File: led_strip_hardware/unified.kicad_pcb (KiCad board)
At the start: 4 copper layers, 48.3 x 20.3 mm, 39 parts, among them P1 mod_jack_in, P2 PWR_TST, P3 LED_STRIP, P4 ICSP, Q1 FDN5618P, SW1 USR_SW, U1 ISL83485IBZ, U2 TPS54560, U3 STM32F030-32, U4 NCP1117ST33T3G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

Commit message: LED strip hardware rev 7; ready for prod?
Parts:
- C1, C10: footprint SM1210 -> Capacitors_SMD:C_1210
- C11, C9: footprint SA0805 -> Capacitors_SMD:C_0805
- C12, C2, C3, C4, C5, C8, R10, R2, R3, R4, R5, R6, R7, R8, R9: footprint SA0402 -> Resistors_SMD:R_0402
- R1, R11, R12: footprint SA0603 -> Resistors_SMD:R_0603
- U4: value NCP1117ST33T3G -> 1117
- moved Q1 0.80 mm to (121.4, 121.4)
- moved C6 0.76 mm to (152.4, 119.9)
- moved D2 0.51 mm to (132.6, 112.8)
- moved R9 0.38 mm to (118.5, 122.2)
- moved R10 0.25 mm to (117.1, 122.2)
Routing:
- net GND: track 115.0 -> 103.8 mm, vias 50 -> 40
- net VPP: track 47.5 -> 37.3 mm, vias 3 -> 4
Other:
- board size 48.3 x 20.3 mm -> 48.3 x 26.9 mm
- board text added: "LUX"

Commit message: More 'final' touches
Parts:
- D1: footprint SA0603_LED -> LEDs:LED_0603
- moved R7 2.54 mm to (154.9, 115.6), turned to 270 degrees
- moved R8 2.54 mm to (154.9, 118.1), turned to 90 degrees
- moved R5 1.40 mm to (128.4, 125.0), turned to 90 degrees
- moved R6 1.14 mm to (127.1, 125.0)
- moved C4 0.13 mm to (130.9, 125.0), turned to 90 degrees
- moved R3 0.13 mm to (129.7, 125.0)
- moved R2 0.13 mm to (125.9, 125.0)
- moved C5 0.13 mm to (132.2, 125.0)
- turned P3 to 90 degrees
- turned R10 to 90 degrees
- turned SW1 to 180 degrees
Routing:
- net VPP: track 37.3 -> 21.9 mm, vias 4 -> 3
- net GND: track 103.8 -> 111.0 mm, vias 40 -> 38
- net Net-(SW1-Pad3): track 4.53 -> 11.3 mm
- net /DAT: track 16.2 -> 15.3 mm
- net /CLK: track 13.2 -> 13.8 mm
- net Net-(R5-Pad2): track 7.17 -> 7.82 mm
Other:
- board size 48.3 x 26.9 mm -> 48.3 x 20.3 mm

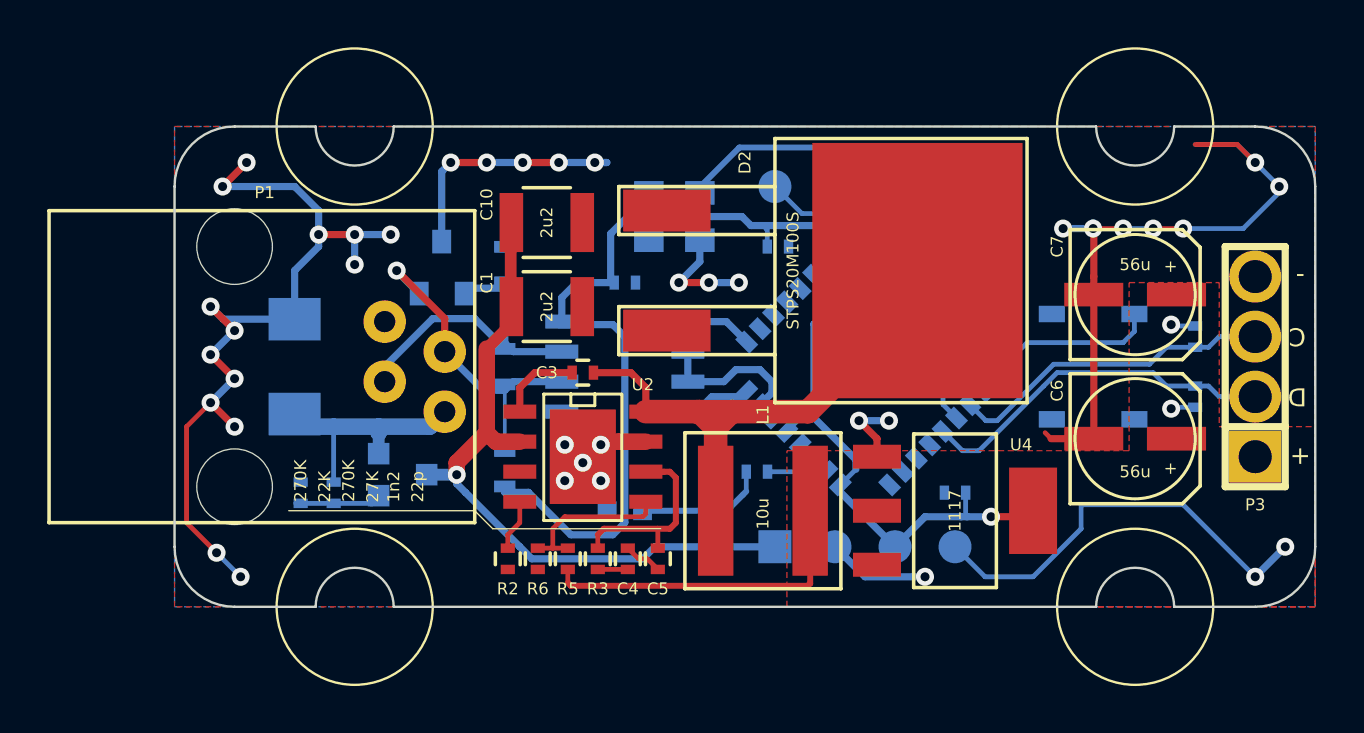
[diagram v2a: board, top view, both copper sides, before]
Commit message: Flipped D2; still need to fix silk bottom
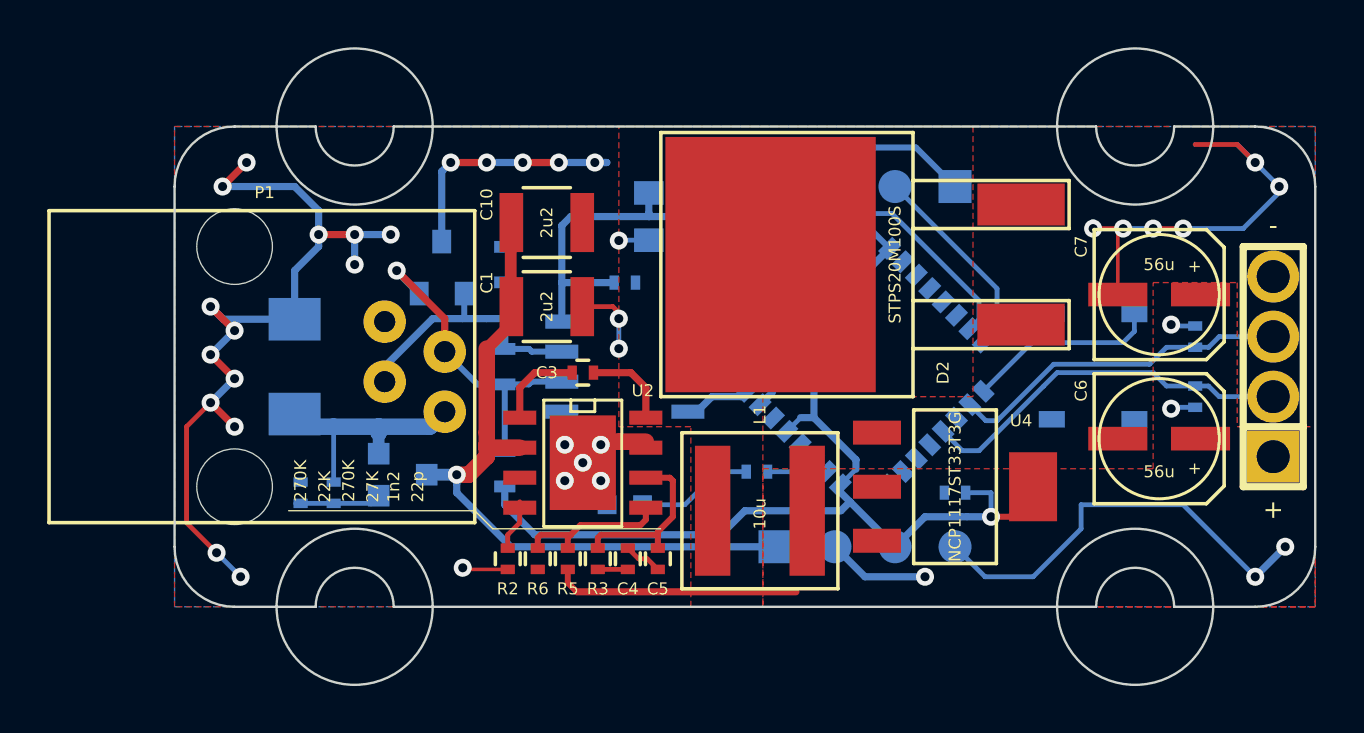
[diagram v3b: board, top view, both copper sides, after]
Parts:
- SW1: value USR_SW -> TL3315NF160Q
- U4: value 1117 -> NCP1117ST33T3G
- moved D2 15.0 mm to (147.6, 112.5), turned to 90 degrees
- moved U4 1.02 mm to (144.8, 121.9)
- moved C6 1.02 mm to (153.4, 119.9)
- moved C7 1.02 mm to (153.4, 113.8)
- moved P3 0.76 mm to (158.2, 116.8)
- moved D1 0.25 mm to (130.8, 122.7)
- moved U2 0.25 mm to (129.0, 120.9)
- moved L1 0.13 mm to (136.5, 122.9)
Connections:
- U3 pad 25: Net-(U3-Pad25) -> Net-(SW1-Pad3)
- U3 pad 27: Net-(SW1-Pad3) -> Net-(U3-Pad27)
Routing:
- net Net-(C3-Pad2): track 24.3 -> 4.40 mm
- net GND: track 111.0 -> 100.3 mm, vias 38 -> 36
- net 3V3: track 78.2 -> 83.8 mm
- net VPP: track 21.9 -> 18.3 mm
- net Net-(SW1-Pad3): track 11.3 -> 8.11 mm
- net Net-(R5-Pad2): track 7.82 -> 6.45 mm
- net Net-(C5-Pad1): track 8.69 -> 7.34 mm
- net /DAT: track 15.3 -> 16.1 mm
- net /CLK: track 13.8 -> 14.6 mm
- net Net-(P1-Pad3): track 13.7 -> 13.0 mm
- net Net-(D1-Pad1): track 5.31 -> 4.71 mm
- added copper zone on F.Cu, net Net-(C3-Pad2)
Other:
- board size 48.3 x 20.3 mm -> 48.3 x 26.9 mm

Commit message: lgtm
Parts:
- U5: value 2CH-TVS -> TVS
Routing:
- net GND: track 100.3 -> 101.8 mm, vias 36 -> 34

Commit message: ship it
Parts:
- U1: value ISL83485IBZ -> ISL83485
- U4: value NCP1117ST33T3G -> NCP1117
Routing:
- net VPP: track 18.3 -> 23.1 mm
- net GND: track 101.8 -> 104.5 mm, vias 34 -> 35
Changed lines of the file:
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@@
     (links 115)
     (no_connects 0)
-    (area 111.709999 103.327999 160.070001 130.352001)
+    (area 97.977143 98.75 160.070001 130.352001)
     (thickness 1.6)
     (drawings 48)
-    (tracks 315)
+    (tracks 323)
     (zones 0)
     (modules 39)
@@
   )
   (setup
-    (last_trace_width 0.1524)
+    (last_trace_width 0.5)
     (user_trace_width 0.2032)
     (user_trace_width 0.254)
@@
     (mod_text_size 0.508 0.508)
     (mod_text_width 0.0762)
-    (pad_size 1.016 2.032)
-    (pad_drill 0)
+    (pad_size 2.2 2.2)
+    (pad_drill 1.4)
     (pad_to_mask_clearance 0)
     (aux_axis_origin 150.622 110.998)
@@
     (fp_circle (center 0 0) (end 0.127 -2.54) (layer F.SilkS) (width 0.127))
     (pad 1 smd rect (at -1.75 0 180) (size 2.5 1) (layers F.Cu F.Paste F.Mask)
-      (net 8 VPP))
+      (net 8 VPP) (thermal_width 0.508))
     (pad 2 smd rect (at 1.75 0 180) (size 2.5 1) (layers F.Cu F.Paste F.Mask)
-      (net 7 GND))
+      (net 7 GND) (thermal_width 0.381))
     (model discret/c_vert_c1v5.wrl
       (at (xyz 0 0 0))
@@
       (effects (font (size 0.508 0.508) (thickness 0.0762)))
     )
-    (fp_text value NCP1117ST33T3G (at 0 0 270) (layer F.SilkS)
+    (fp_text value NCP1117 (at 0 0 270) (layer F.SilkS)
       (effects (font (size 0.508 0.508) (thickness 0.0762)))
     )
@@
     (fp_circle (center 0 0) (end 0.127 -2.54) (layer F.SilkS) (width 0.127))
     (pad 1 smd rect (at -1.75 0 180) (size 2.5 1) (layers F.Cu F.Paste F.Mask)
-      (net 8 VPP))
+      (net 8 VPP) (thermal_width 0.381))
     (pad 2 smd rect (at 1.75 0 180) (size 2.5 1) (layers F.Cu F.Paste F.Mask)
-      (net 7 GND))
+      (net 7 GND) (thermal_width 0.381))
     (model discret/c_vert_c1v5.wrl
       (at (xyz 0 0 0))
@@
     (fp_line (start -2.54 1.27) (end -2.54 -1.27) (layer F.SilkS) (width 0.3048))
     (pad 1 thru_hole rect (at -3.81 0 90) (size 2.2 2.2) (drill 1.4) (layers *.Cu *.Mask F.SilkS)
-      (net 8 VPP) (thermal_width 1.27))
+      (net 8 VPP) (zone_connect 1) (thermal_width 1.27))
     (pad 2 thru_hole circle (at -1.27 0 90) (size 2.2 2.2) (drill 1.4) (layers *.Cu *.Mask F.SilkS)
       (net 3 /DAT))
@@
       (effects (font (size 0.508 0.508) (thickness 0.0762)) (justify mirror))
     )
-    (fp_text value ISL83485IBZ (at 0 -1.016 270) (layer B.SilkS)
+    (fp_text value ISL83485 (at 0 -1.016 270) (layer B.SilkS)
       (effects (font (size 0.508 0.508) (thickness 0.0762)) (justify mirror))
     )
@@
   (segment (start 140.589 120.777) (end 140.589 121.180797) (width 0.3048) (layer B.Cu) (net 6))
   (segment (start 138.811 118.999) (end 140.589 120.777) (width 0.3048) (layer B.Cu) (net 6))
+  (segment (start 131.699 120.269) (end 129.667 120.269) (width 0.5) (layer F.Cu) (net 7) (status C00000))
+  (segment (start 129.667 120.269) (end 129.032 120.904) (width 0.5) (layer F.Cu) (net 7) (status C00000))
+  (segment (start 151.666 119.888) (end 151.666 118.519) (width 0.1524) (layer F.Cu) (net 7))
+  (via (at 151.003 118.237) (size 0.762) (drill 0.381) (layers F.Cu B.Cu) (net 7))
+  (segment (start 151.384 118.237) (end 151.003 118.237) (width 0.1524) (layer F.Cu) (net 7))
+  (segment (start 151.666 118.519) (end 151.384 118.237) (width 0.1524) (layer F.Cu) (net 7))
   (segment (start 128.143 118.745) (end 129.921 118.745) (width 0.2032) (layer B.Cu) (net 7))
   (via (at 130.429 116.078) (size 0.762) (drill 0.381) (layers F.Cu B.Cu) (net 7))
@@
   (via (at 123.952 125.349) (size 0.762) (drill 0.381) (layers F.Cu B.Cu) (net 7))
   (segment (start 125.857 125.418) (end 124.021 125.418) (width 0.1524) (layer F.Cu) (net 7))
-  (segment (start 151.666 113.792) (end 151.666 111.224) (width 0.1524) (layer F.Cu) (net 7))
+  (segment (start 151.666 113.792) (end 151.666 111.224) (width 0.1524) (layer F.Cu) (net 7) (status 10))
   (segment (start 151.666 111.224) (end 151.892 110.998) (width 0.1524) (layer F.Cu) (net 7))
   (segment (start 157.48 108.204) (end 156.718 107.442) (width 0.2032) (layer B.Cu) (net 7))
@@
   (segment (start 119.38 111.252) (end 119.38 112.522) (width 0.3048) (layer B.Cu) (net 7))
   (via (at 119.38 112.522) (size 0.762) (drill 0.381) (layers F.Cu B.Cu) (net 7))
-  (segment (start 116.84 109.22) (end 113.792 109.22) (width 0.3048) (layer B.Cu) (net 7))
+  (segment (start 116.205 109.22) (end 113.792 109.22) (width 0.3048) (layer B.Cu) (net 7))
   (via (at 113.792 109.22) (size 0.762) (drill 0.381) (layers F.Cu B.Cu) (net 7))
   (segment (start 113.792 109.22) (end 114.808 108.204) (width 0.3048) (layer F.Cu) (net 7))
   (via (at 114.808 108.204) (size 0.762) (drill 0.381) (layers F.Cu B.Cu) (net 7))
-  (segment (start 117.856 110.236) (end 117.856 111.252) (width 0.3048) (layer B.Cu) (net 7))
-  (segment (start 117.856 110.236) (end 116.84 109.22) (width 0.3048) (layer B.Cu) (net 7))
+  (segment (start 117.856 110.871) (end 117.856 111.252) (width 0.3048) (layer B.Cu) (net 7))
+  (segment (start 117.856 110.871) (end 116.205 109.22) (width 0.3048) (layer B.Cu) (net 7))
   (segment (start 116.84 114.8334) (end 113.8174 114.8334) (width 0.3048) (layer B.Cu) (net 7))
   (via (at 114.3 119.38) (size 0.762) (drill 0.381) (layers F.Cu B.Cu) (net 7))
@@
   (via (at 129.794 121.666) (size 0.762) (drill 0.381) (layers F.Cu B.Cu) (net 7))
   (via (at 129.794 120.142) (size 0.762) (drill 0.381) (layers F.Cu B.Cu) (net 7))
-  (segment (start 131.699 120.015) (end 130.556 120.015) (width 0.7) (layer F.Cu) (net 7))
-  (segment (start 130.556 120.015) (end 129.667 120.015) (width 0.7) (layer F.Cu) (net 7))
   (segment (start 129.667 120.015) (end 129.032 120.65) (width 0.7) (layer F.Cu) (net 7))
+  (segment (start 155.166 119.888) (end 156.845 119.888) (width 0.3048) (layer F.Cu) (net 8))
+  (segment (start 158.242 120.65) (end 156.845 120.65) (width 0.1524) (layer F.Cu) (net 8))
+  (segment (start 156.845 120.65) (end 156.845 119.888) (width 0.1524) (layer F.Cu) (net 8))
+  (segment (start 156.845 119.888) (end 156.845 118.999) (width 0.3048) (layer F.Cu) (net 8))
   (segment (start 154.94 118.56) (end 153.982 118.56) (width 0.2032) (layer B.Cu) (net 8))
   (via (at 153.924 118.618) (size 0.762) (drill 0.381) (layers F.Cu B.Cu) (net 8))
@@
     (polygon
       (pts
-        (xy 155.956 127) (xy 136.652 127) (xy 136.652 121.158) (xy 153.162 121.158) (xy 153.162 113.284)
-        (xy 156.718 113.284) (xy 156.718 119.38) (xy 160.02 119.38) (xy 160.02 127) (xy 155.956 127)
+        (xy 155.956 127) (xy 136.652 127) (xy 136.652 121.158) (xy 153.543 121.158) (xy 153.543 112.522)
+        (xy 156.972 112.522) (xy 156.972 119.38) (xy 160.02 119.38) (xy 160.02 127) (xy 155.956 127)
       )
     )

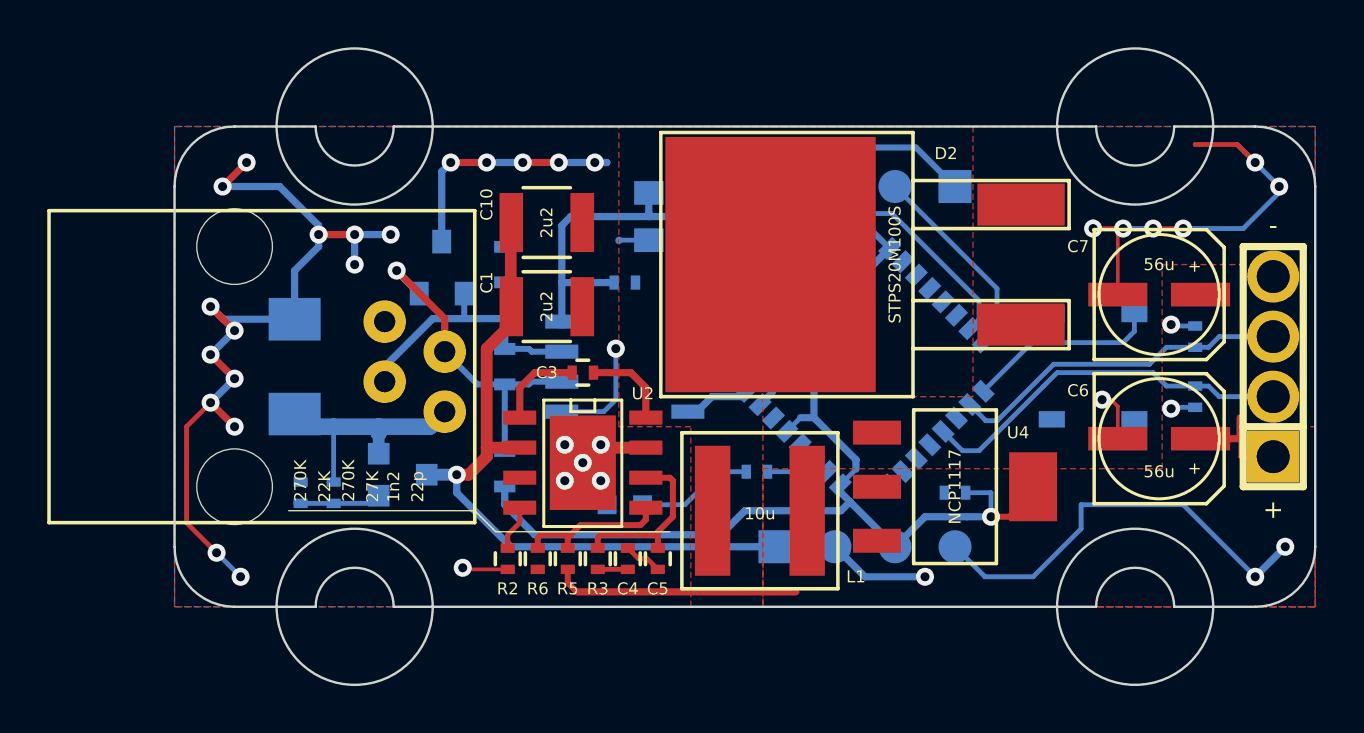
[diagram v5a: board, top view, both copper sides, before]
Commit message: Copper for the hub
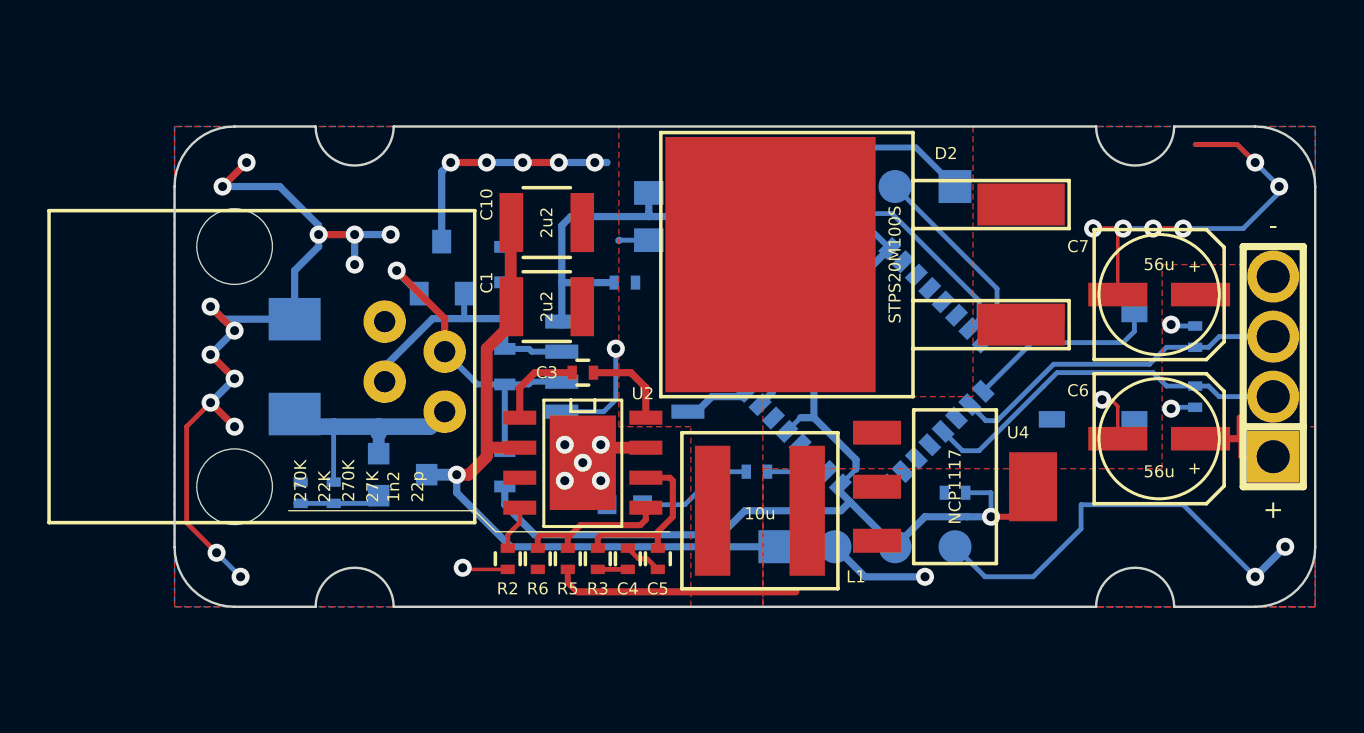
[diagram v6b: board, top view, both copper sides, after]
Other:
- board size 48.3 x 26.9 mm -> 48.3 x 20.3 mm
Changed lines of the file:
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@@
     (links 115)
     (no_connects 0)
-    (area 97.977143 98.75 160.070001 130.352001)
+    (area 111.709999 106.629999 160.070001 127.050001)
     (thickness 1.6)
     (drawings 48)
@@
   (gr_line (start 124.46 122.936) (end 116.586 122.936) (angle 90) (layer F.SilkS) (width 0.0508))
   (gr_line (start 125.222 123.698) (end 124.46 122.936) (angle 90) (layer F.SilkS) (width 0.0508))
-  (gr_circle (center 119.38 127) (end 122.682 127) (layer Edge.Cuts) (width 0.1))
-  (gr_circle (center 152.4 127) (end 155.702 127) (layer Edge.Cuts) (width 0.1))
-  (gr_circle (center 152.4 106.68) (end 155.702 106.68) (layer Edge.Cuts) (width 0.1))
-  (gr_circle (center 119.38 106.68) (end 122.682 106.68) (layer Edge.Cuts) (width 0.1))
+  (gr_circle (center 119.38 127) (end 122.682 127) (layer Dwgs.User) (width 0.1))
+  (gr_circle (center 152.4 127) (end 155.702 127) (layer Dwgs.User) (width 0.1))
+  (gr_circle (center 152.4 106.68) (end 155.702 106.68) (layer Dwgs.User) (width 0.1))
+  (gr_circle (center 119.38 106.68) (end 122.682 106.68) (layer Dwgs.User) (width 0.1))
   (gr_text "Digital LED Strip\nrev 7" (at 152.4 111.76) (layer B.SilkS)
     (effects (font (size 0.762 0.762) (thickness 0.13)) (justify mirror))

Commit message: LED Strip rev 8
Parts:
- C1, C10: value 2u2 -> 4u7
- C2, C8: footprint Resistors_SMD:R_0402 -> Capacitors_SMD:C_0402
- C6, C7: value 56u -> 82u
- L1: value 10u -> XAL6060 103
- Q1: value FDN5618P -> CPH3351
- R5: value 270K -> 68K
- R6: value 22K -> 12K
- U1: value ISL83485 -> ISL83485IBZ
- U5: value TVS -> TPD2E2U06
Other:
- board text added: "Digital LED Strip rev 8"
- board text removed: "Digital LED Strip rev 7"
